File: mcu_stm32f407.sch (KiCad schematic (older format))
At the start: 24 parts, among them J1 Conn_01x05_Male, U1 STM32F407VGTx, Y1 8MHz

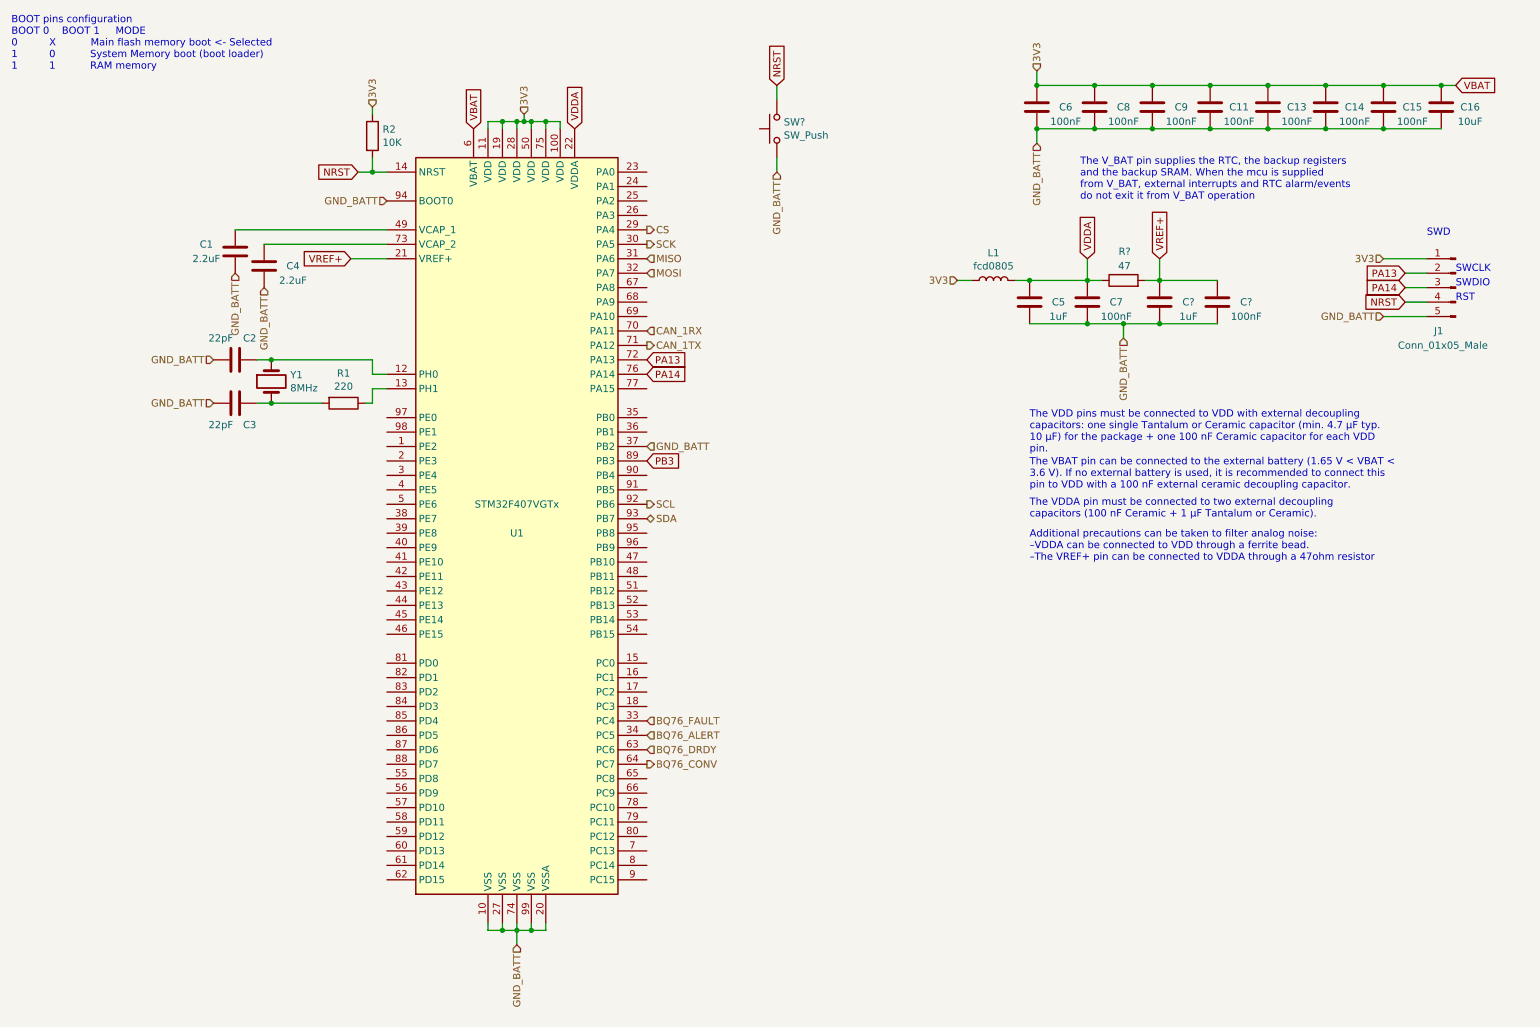
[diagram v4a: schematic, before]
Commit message: Dletes hw_balanceo folder
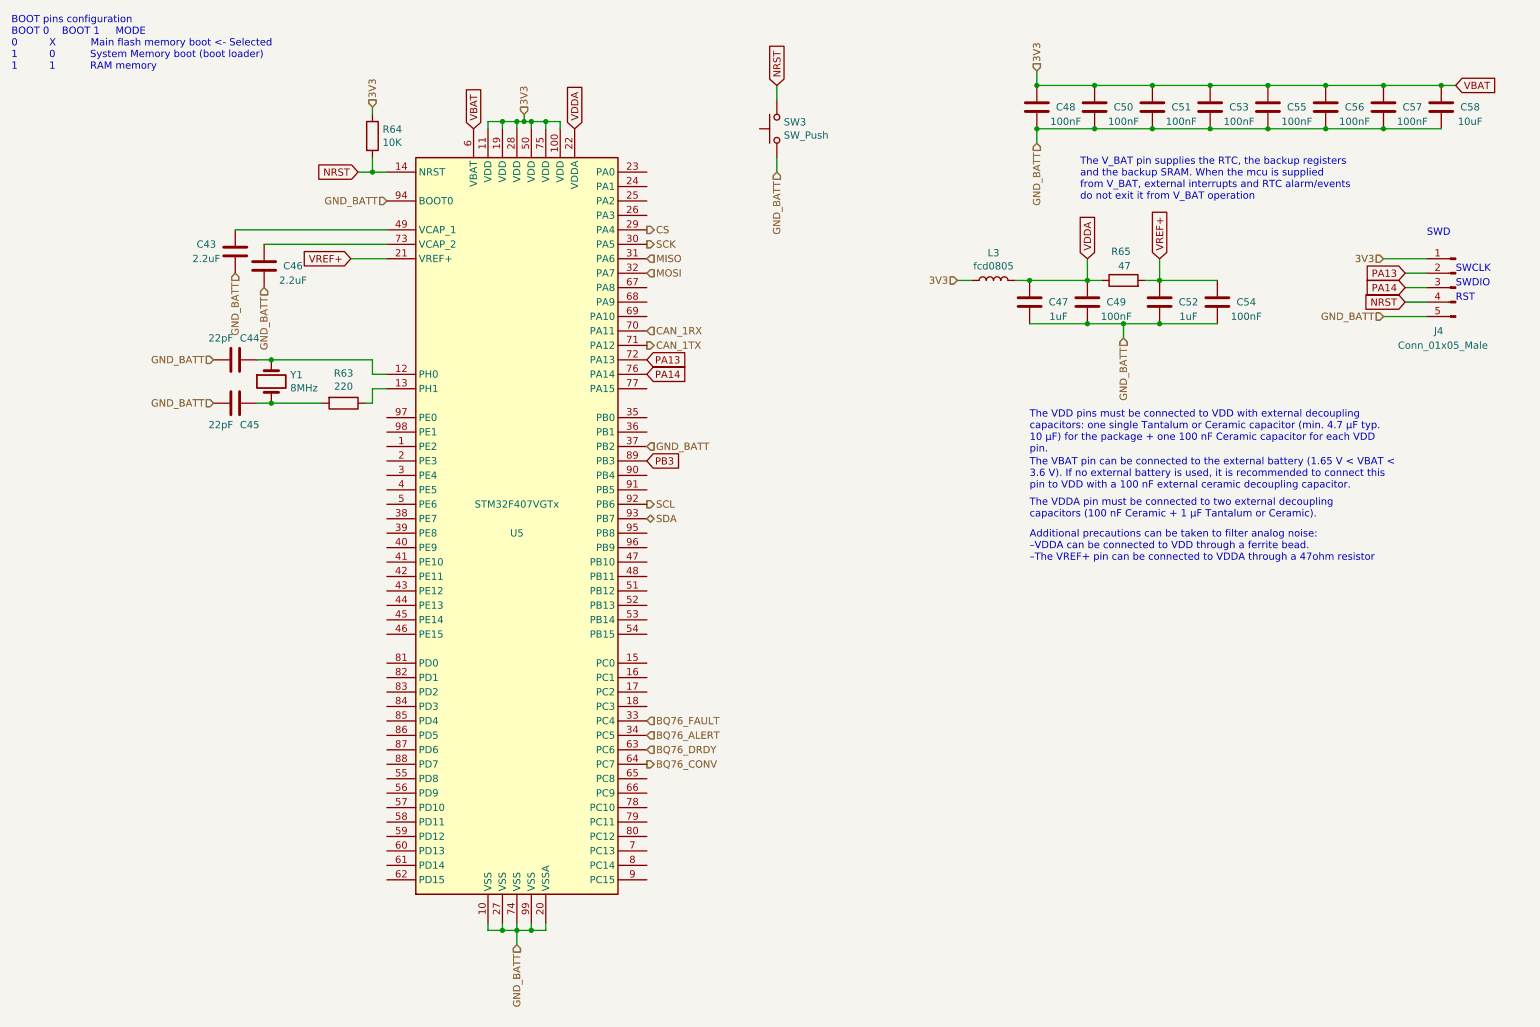
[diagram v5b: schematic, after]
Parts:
- gave numbers to parts that had none: 4
- renumbered C1 to C43, C2 to C44, C3 to C45, C4 to C46, C5 to C47, C6 to C48, C7 to C49, C8 to C50, C9 to C51, C11 to C53, C13 to C55, C14 to C56, C15 to C57, C16 to C58, J1 to J4, L1 to L3, R1 to R63, R2 to R64, U1 to U5
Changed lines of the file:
@@
 $EndDescr
 $Comp
-L MCU_ST_STM32F4:STM32F407VGTx U1
+L MCU_ST_STM32F4:STM32F407VGTx U5
 U 1 1 5FE4F27B
 P 4050 4000
-F 0 "U1" H 4050 3900 50  0000 C CNN
+F 0 "U5" H 4050 3900 50  0000 C CNN
 F 1 "STM32F407VGTx" H 4050 4100 50  0000 C CNN
 F 2 "Package_QFP:LQFP-100_14x14mm_P0.5mm" H 3350 1400 50  0001 R CNN
@@
 $EndComp
 $Comp
-L Device:C C3
+L Device:C C45
 U 1 1 5FE53997
 P 2100 3200
-F 0 "C3" V 1950 3100 50  0000 C CNN
+F 0 "C45" V 1950 3100 50  0000 C CNN
 F 1 "22pF" V 1950 3300 50  0000 C CNN
 F 2 "Capacitor_SMD:C_0805_2012Metric_Pad1.18x1.45mm_HandSolder" H 2138 3050 50  0001 C CNN
@@
 $EndComp
 $Comp
-L Device:C C2
+L Device:C C44
 U 1 1 5FE54349
 P 2100 2900
-F 0 "C2" V 2250 2800 50  0000 C CNN
+F 0 "C44" V 2250 2800 50  0000 C CNN
 F 1 "22pF" V 2250 3000 50  0000 C CNN
 F 2 "Capacitor_SMD:C_0805_2012Metric_Pad1.18x1.45mm_HandSolder" H 2138 2750 50  0001 C CNN
@@
 	4050 6850 4050 6950
 $Comp
-L Device:C C1
+L Device:C C43
 U 1 1 5FE5A7A2
 P 2100 2150
-F 0 "C1" H 1900 2200 50  0000 C CNN
+F 0 "C43" H 1900 2200 50  0000 C CNN
 F 1 "2.2uF" H 1900 2100 50  0000 C CNN
 F 2 "Capacitor_SMD:C_0805_2012Metric_Pad1.18x1.45mm_HandSolder" H 2138 2000 50  0001 C CNN
@@
 $EndComp
 $Comp
-L Device:C C4
+L Device:C C46
 U 1 1 5FE5B890
 P 2300 2250
-F 0 "C4" H 2500 2250 50  0000 C CNN
+F 0 "C46" H 2500 2250 50  0000 C CNN
 F 1 "2.2uF" H 2500 2150 50  0000 C CNN
 F 2 "Capacitor_SMD:C_0805_2012Metric_Pad1.18x1.45mm_HandSolder" H 2338 2100 50  0001 C CNN
@@
 	4250 1250 4350 1250
 $Comp
-L Device:R R1
+L Device:R R63
 U 1 1 5FE6766C
 P 2850 3200
-F 0 "R1" V 2643 3200 50  0000 C CNN
+F 0 "R63" V 2643 3200 50  0000 C CNN
 F 1 "220" V 2734 3200 50  0000 C CNN
 F 2 "Resistor_SMD:R_0805_2012Metric_Pad1.20x1.40mm_HandSolder" V 2780 3200 50  0001 C CNN
@@
 VBAT
 $Comp
-L Device:C C6
+L Device:C C48
 U 1 1 5FE7DFED
 P 7650 1150
-F 0 "C6" H 7850 1150 50  0000 C CNN
+F 0 "C48" H 7850 1150 50  0000 C CNN
 F 1 "100nF" H 7850 1050 50  0000 C CNN
 F 2 "Capacitor_SMD:C_0805_2012Metric_Pad1.18x1.45mm_HandSolder" H 7688 1000 50  0001 C CNN
@@
 $EndComp
 $Comp
-L Device:C C8
+L Device:C C50
 U 1 1 5FE7E489
 P 8050 1150
-F 0 "C8" H 8250 1150 50  0000 C CNN
+F 0 "C50" H 8250 1150 50  0000 C CNN
 F 1 "100nF" H 8250 1050 50  0000 C CNN
 F 2 "Capacitor_SMD:C_0805_2012Metric_Pad1.18x1.45mm_HandSolder" H 8088 1000 50  0001 C CNN
@@
 $EndComp
 $Comp
-L Device:C C9
+L Device:C C51
 U 1 1 5FE7E74E
 P 8450 1150
-F 0 "C9" H 8650 1150 50  0000 C CNN
+F 0 "C51" H 8650 1150 50  0000 C CNN
 F 1 "100nF" H 8650 1050 50  0000 C CNN
 F 2 "Capacitor_SMD:C_0805_2012Metric_Pad1.18x1.45mm_HandSolder" H 8488 1000 50  0001 C CNN
@@
 $EndComp
 $Comp
-L Device:C C11
+L Device:C C53
 U 1 1 5FE7E947
 P 8850 1150
-F 0 "C11" H 9050 1150 50  0000 C CNN
+F 0 "C53" H 9050 1150 50  0000 C CNN
 F 1 "100nF" H 9050 1050 50  0000 C CNN
 F 2 "Capacitor_SMD:C_0805_2012Metric_Pad1.18x1.45mm_HandSolder" H 8888 1000 50  0001 C CNN
@@
 	8850 1000 9250 1000
 $Comp
-L Device:C C16
+L Device:C C58
 U 1 1 5FE8634C
 P 10450 1150
-F 0 "C16" H 10650 1150 50  0000 C CNN
+F 0 "C58" H 10650 1150 50  0000 C CNN
 F 1 "10uF" H 10650 1050 50  0000 C CNN
 F 2 "Capacitor_SMD:C_0805_2012Metric_Pad1.18x1.45mm_HandSolder" H 10488 1000 50  0001 C CNN
@@
 $EndComp
 $Comp
-L Device:C C15
+L Device:C C57
 U 1 1 5FE86346
 P 10050 1150
-F 0 "C15" H 10250 1150 50  0000 C CNN
+F 0 "C57" H 10250 1150 50  0000 C CNN
 F 1 "100nF" H 10250 1050 50  0000 C CNN
 F 2 "Capacitor_SMD:C_0805_2012Metric_Pad1.18x1.45mm_HandSolder" H 10088 1000 50  0001 C CNN
@@
 $EndComp
 $Comp
-L Device:C C14
+L Device:C C56
 U 1 1 5FE86340
 P 9650 1150
-F 0 "C14" H 9850 1150 50  0000 C CNN
+F 0 "C56" H 9850 1150 50  0000 C CNN
 F 1 "100nF" H 9850 1050 50  0000 C CNN
 F 2 "Capacitor_SMD:C_0805_2012Metric_Pad1.18x1.45mm_HandSolder" H 9688 1000 50  0001 C CNN
@@
 $EndComp
 $Comp
-L Device:C C13
+L Device:C C55
 U 1 1 5FE8633A
 P 9250 1150
-F 0 "C13" H 9450 1150 50  0000 C CNN
+F 0 "C55" H 9450 1150 50  0000 C CNN
 F 1 "100nF" H 9450 1050 50  0000 C CNN
 F 2 "Capacitor_SMD:C_0805_2012Metric_Pad1.18x1.45mm_HandSolder" H 9288 1000 50  0001 C CNN
@@
 VDDA
 $Comp
-L Device:C C5
+L Device:C C47
 U 1 1 5FEB5513
 P 7600 2500
-F 0 "C5" H 7800 2500 50  0000 C CNN
+F 0 "C47" H 7800 2500 50  0000 C CNN
 F 1 "1uF" H 7800 2400 50  0000 C CNN
 F 2 "Capacitor_SMD:C_0805_2012Metric_Pad1.18x1.45mm_HandSolder" H 7638 2350 50  0001 C CNN
@@
 $EndComp
 $Comp
-L Device:C C7
+L Device:C C49
 U 1 1 5FEB5519
 P 8000 2500
-F 0 "C7" H 8200 2500 50  0000 C CNN
+F 0 "C49" H 8200 2500 50  0000 C CNN
 F 1 "100nF" H 8200 2400 50  0000 C CNN
 F 2 "Capacitor_SMD:C_0805_2012Metric_Pad1.18x1.45mm_HandSolder" H 8038 2350 50  0001 C CNN
@@
 PB3
 $Comp
-L Device:L L1
+L Device:L L3
 U 1 1 5FEED219
 P 7350 2350
-F 0 "L1" V 7540 2350 50  0000 C CNN
+F 0 "L3" V 7540 2350 50  0000 C CNN
 F 1 "fcd0805" V 7449 2350 50  0000 C CNN
 F 2 "Inductor_SMD:L_0805_2012Metric_Pad1.05x1.20mm_HandSolder" H 7350 2350 50  0001 C CNN
@@
 PA14
 $Comp
-L Connector:Conn_01x05_Male J1
+L Connector:Conn_01x05_Male J4
 U 1 1 5FF02221
 P 10550 2400
-F 0 "J1" H 10700 2100 50  0000 R CNN
+F 0 "J4" H 10700 2100 50  0000 R CNN
 F 1 "Conn_01x05_Male" H 10950 2000 50  0000 R CNN
 F 2 "Connector_PinHeader_2.54mm:PinHeader_1x05_P2.54mm_Vertical" H 10550 2400 50  0001 C CNN
@@
 	10050 2600 10350 2600
 $Comp
-L Device:R R2
+L Device:R R64
 U 1 1 5FF0D03B
 P 3050 1350
-F 0 "R2" H 3120 1396 50  0000 L CNN
+F 0 "R64" H 3120 1396 50  0000 L CNN
 F 1 "10K" H 3120 1305 50  0000 L CNN
 F 2 "Resistor_SMD:R_0805_2012Metric_Pad1.20x1.40mm_HandSolder" V 2980 1350 50  0001 C CNN
@@
 GND_BATT
 $Comp
-L Switch:SW_Push SW?
+L Switch:SW_Push SW3
 U 1 1 6020B6D3
 P 5850 1300
-F 0 "SW?" V 5896 1252 50  0000 R CNN
+F 0 "SW3" V 5896 1252 50  0000 R CNN
 F 1 "SW_Push" V 5805 1252 50  0000 R CNN
 F 2 "" H 5850 1500 50  0001 C CNN
@@
 VREF+
 $Comp
-L Device:R R?
+L Device:R R65
 U 1 1 6023C24E
 P 8250 2350
-F 0 "R?" V 8450 2300 50  0000 L CNN
+F 0 "R65" V 8450 2300 50  0000 L CNN
 F 1 "47" V 8350 2300 50  0000 L CNN
 F 2 "" V 8180 2350 50  0001 C CNN
@@
 	8500 2350 8400 2350
 $Comp
-L Device:C C?
+L Device:C C52
 U 1 1 60267A98
 P 8500 2500
-F 0 "C?" H 8700 2500 50  0000 C CNN
+F 0 "C52" H 8700 2500 50  0000 C CNN
 F 1 "1uF" H 8700 2400 50  0000 C CNN
 F 2 "Capacitor_SMD:C_0805_2012Metric_Pad1.18x1.45mm_HandSolder" H 8538 2350 50  0001 C CNN
@@
 Connection ~ 7600 2350
 $Comp
-L Device:C C?
+L Device:C C54
 U 1 1 60267A9E
 P 8900 2500
-F 0 "C?" H 9100 2500 50  0000 C CNN
+F 0 "C54" H 9100 2500 50  0000 C CNN
 F 1 "100nF" H 9100 2400 50  0000 C CNN
 F 2 "Capacitor_SMD:C_0805_2012Metric_Pad1.18x1.45mm_HandSolder" H 8938 2350 50  0001 C CNN

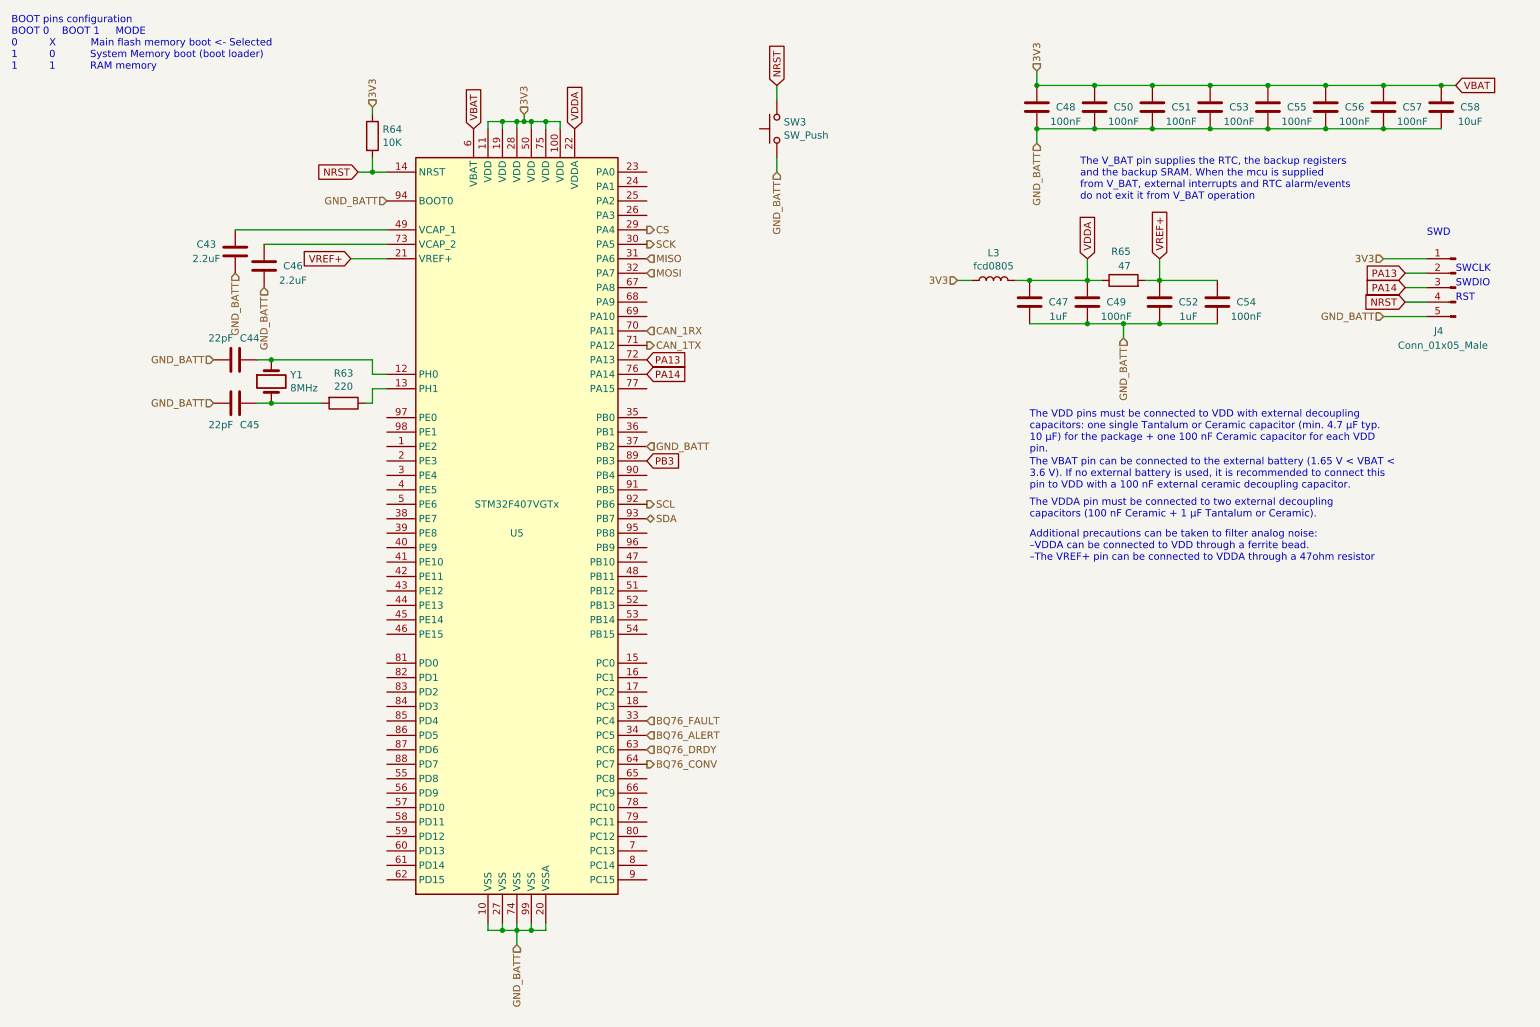
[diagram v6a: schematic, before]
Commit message: Fixes missing footprints, adds initial pcb
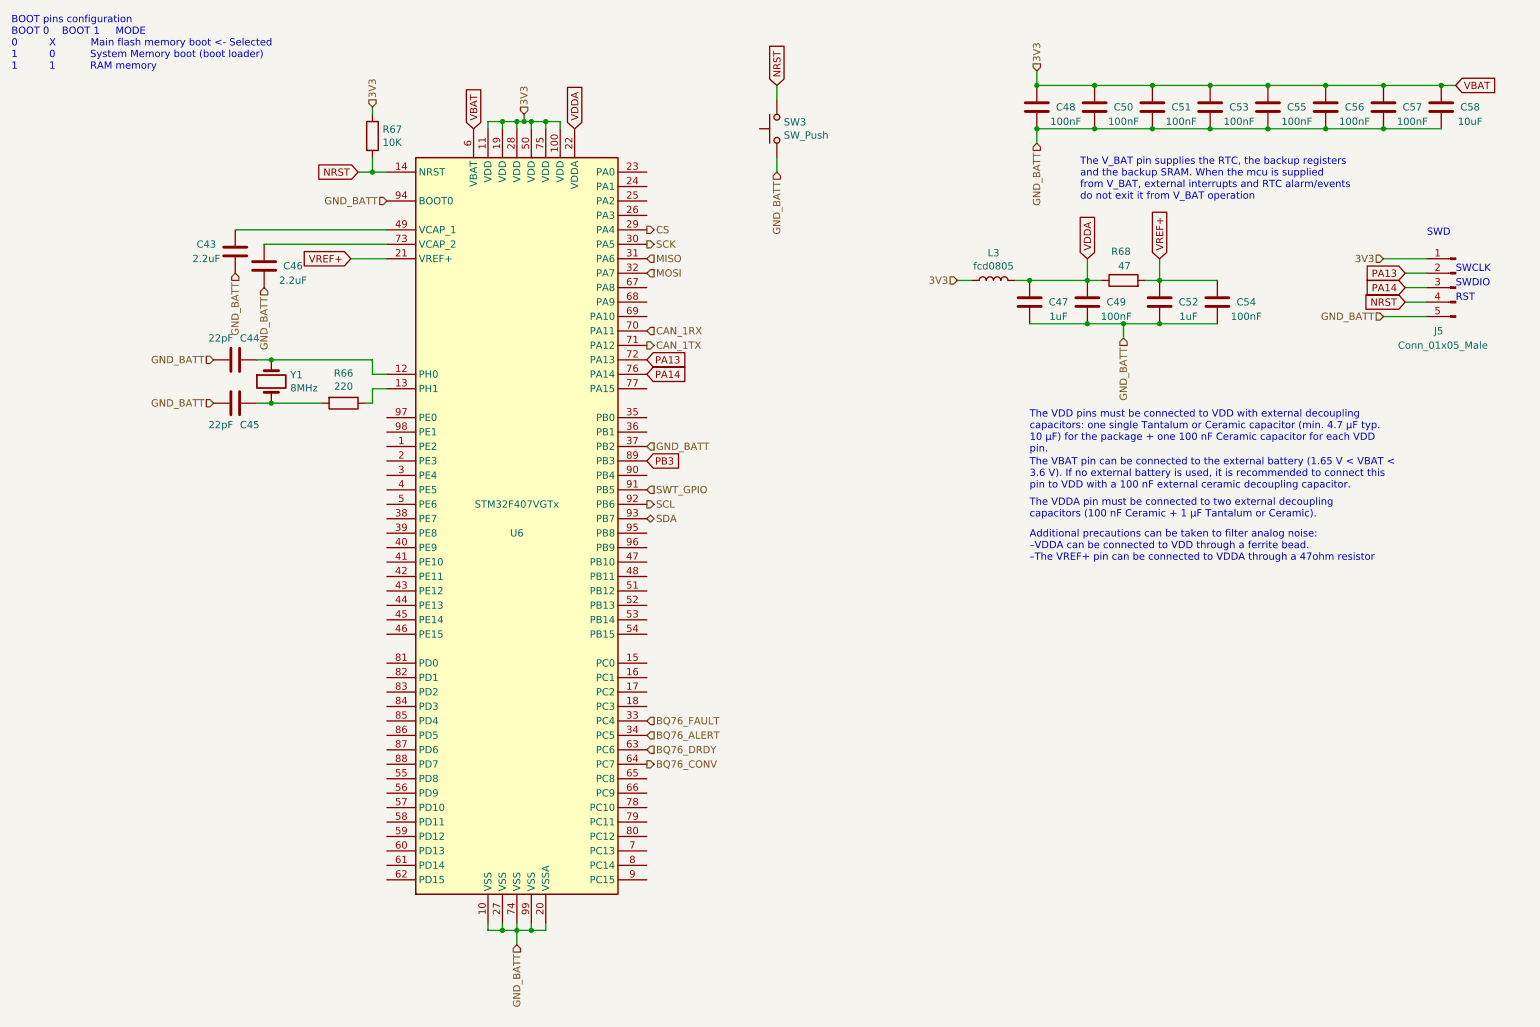
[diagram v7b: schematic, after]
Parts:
- R68: renamed from R65; footprint (none) -> Resistor_SMD:R_0805_2012Metric_Pad1.20x1.40mm_HandSolder
- SW3: footprint (none) -> Button_Switch_SMD:SW_SPST_TL3305A
- renumbered J4 to J5, R63 to R66, R64 to R67, U5 to U6
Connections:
- net SWT_GPIO: now reaches U6.91 (PB5)
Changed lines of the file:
@@
 $Descr A4 11693 8268
 encoding utf-8
-Sheet 7 8
+Sheet 8 8
 Title ""
 Date ""
@@
 $EndDescr
 $Comp
-L MCU_ST_STM32F4:STM32F407VGTx U5
+L MCU_ST_STM32F4:STM32F407VGTx U6
 U 1 1 5FE4F27B
 P 4050 4000
-F 0 "U5" H 4050 3900 50  0000 C CNN
+F 0 "U6" H 4050 3900 50  0000 C CNN
 F 1 "STM32F407VGTx" H 4050 4100 50  0000 C CNN
 F 2 "Package_QFP:LQFP-100_14x14mm_P0.5mm" H 3350 1400 50  0001 R CNN
@@
 	4250 1250 4350 1250
 $Comp
-L Device:R R63
+L Device:R R66
 U 1 1 5FE6766C
 P 2850 3200
-F 0 "R63" V 2643 3200 50  0000 C CNN
+F 0 "R66" V 2643 3200 50  0000 C CNN
 F 1 "220" V 2734 3200 50  0000 C CNN
 F 2 "Resistor_SMD:R_0805_2012Metric_Pad1.20x1.40mm_HandSolder" V 2780 3200 50  0001 C CNN
@@
 PA14
 $Comp
-L Connector:Conn_01x05_Male J4
+L Connector:Conn_01x05_Male J5
 U 1 1 5FF02221
 P 10550 2400
-F 0 "J4" H 10700 2100 50  0000 R CNN
+F 0 "J5" H 10700 2100 50  0000 R CNN
 F 1 "Conn_01x05_Male" H 10950 2000 50  0000 R CNN
 F 2 "Connector_PinHeader_2.54mm:PinHeader_1x05_P2.54mm_Vertical" H 10550 2400 50  0001 C CNN
@@
 	10050 2600 10350 2600
 $Comp
-L Device:R R64
+L Device:R R67
 U 1 1 5FF0D03B
 P 3050 1350
-F 0 "R64" H 3120 1396 50  0000 L CNN
+F 0 "R67" H 3120 1396 50  0000 L CNN
 F 1 "10K" H 3120 1305 50  0000 L CNN
 F 2 "Resistor_SMD:R_0805_2012Metric_Pad1.20x1.40mm_HandSolder" V 2980 1350 50  0001 C CNN
@@
 F 0 "SW3" V 5896 1252 50  0000 R CNN
 F 1 "SW_Push" V 5805 1252 50  0000 R CNN
-F 2 "" H 5850 1500 50  0001 C CNN
+F 2 "Button_Switch_SMD:SW_SPST_TL3305A" H 5850 1500 50  0001 C CNN
 F 3 "~" H 5850 1500 50  0001 C CNN
 	1    5850 1300
@@
 VREF+
 $Comp
-L Device:R R65
+L Device:R R68
 U 1 1 6023C24E
 P 8250 2350
-F 0 "R65" V 8450 2300 50  0000 L CNN
+F 0 "R68" V 8450 2300 50  0000 L CNN
 F 1 "47" V 8350 2300 50  0000 L CNN
-F 2 "" V 8180 2350 50  0001 C CNN
+F 2 "Resistor_SMD:R_0805_2012Metric_Pad1.20x1.40mm_HandSolder" V 8180 2350 50  0001 C CNN
 F 3 "~" H 8250 2350 50  0001 C CNN
 	1    8250 2350
@@
 Text Notes 7600 4300 0    50   ~ 0
 Additional precautions can be taken to filter analog noise:\n–VDDA can be connected to VDD through a ferrite bead.\n–The VREF+ pin can be connected to VDDA through a 47ohm resistor
+Text HLabel 4950 3800 2    50   Input ~ 0
+SWT_GPIO
 $EndSCHEMATC
